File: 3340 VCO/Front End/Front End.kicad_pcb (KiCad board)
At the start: 2 copper layers, 60.6 x 104.5 mm, 32 parts, among them J1 AudioJack2_SwitchT, J2 AudioJack2_SwitchT, J3 AudioJack2_SwitchT, J4 AudioJack2_SwitchT, J5 AudioJack2_SwitchT, J6 Conn_01x19, J7 AudioJack2_SwitchT, J8 AudioJack2_SwitchT, J9 AudioJack2_SwitchT, SW1 SW_SPDT

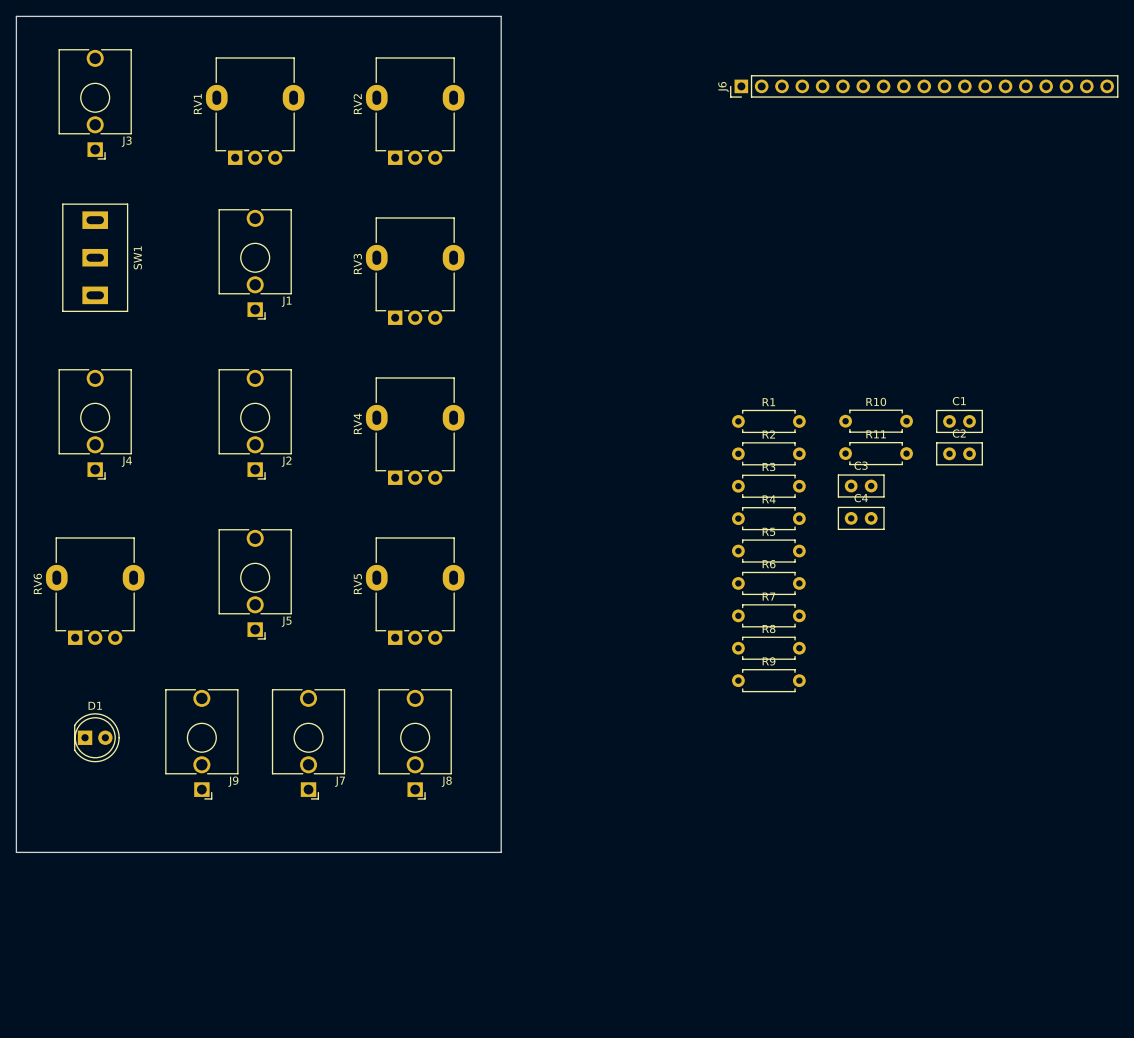
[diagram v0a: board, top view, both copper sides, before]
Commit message: Arrange VCO front end components
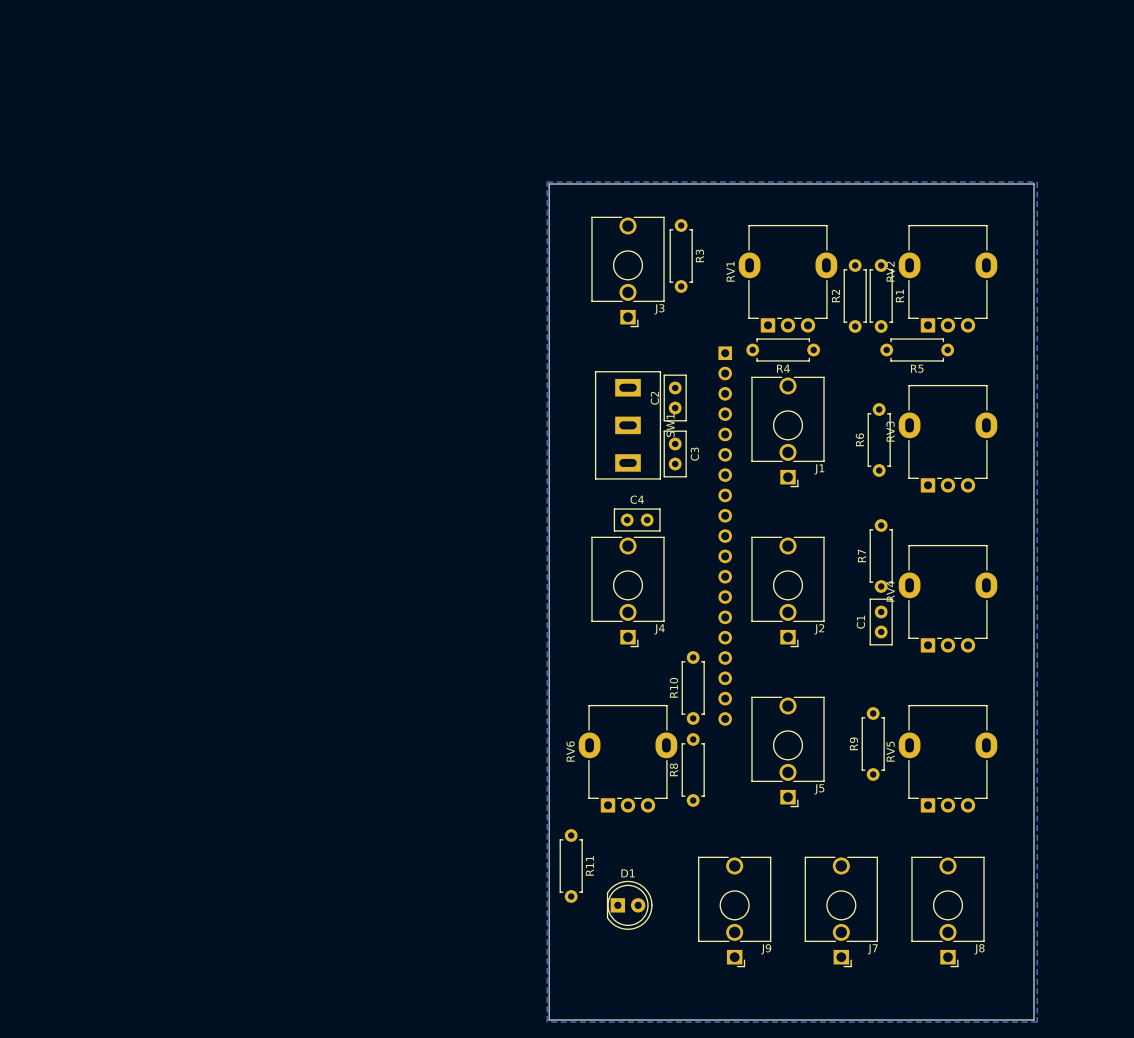
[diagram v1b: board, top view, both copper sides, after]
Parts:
- J6: moved to B.Cu
- moved D1 69.8 mm to (112.3, 137.4)
- moved J1 69.8 mm to (133.6, 83.8)
- moved J2 69.8 mm to (133.6, 103.8)
- moved J3 69.8 mm to (113.6, 63.9)
- moved J4 69.8 mm to (113.6, 103.8)
- moved J5 69.8 mm to (133.6, 123.8)
- moved J8 69.8 mm to (153.6, 143.8)
- moved J9 69.8 mm to (126.9, 143.8)
- moved RV1 69.8 mm to (131.1, 64.9)
- moved RV2 69.8 mm to (151.1, 64.9)
- moved RV3 69.8 mm to (151.1, 84.9)
- moved RV4 69.8 mm to (151.1, 104.9)
- moved RV5 69.8 mm to (151.1, 124.9)
- moved RV6 69.8 mm to (111.1, 124.9)
- moved SW1 69.8 mm to (113.6, 77.4)
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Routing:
- added copper zone on B.Cu, net Chassis

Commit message: Update VCO capacitor selection
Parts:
- added H1: MNT_STANDOFF, 0_MountingHole:MountingHole_Pitch7.5mm_Drill3.4mm, F.Cu at (109.5, 146.2)
- added H2: MNT_STANDOFF, 0_MountingHole:MountingHole_Pitch7.5mm_Drill3.4mm, F.Cu at (143.0, 70.5)
- C2: footprint 0_Capacitor_THT:C_Disc_D5.5mm_W2.5mm_P2.50mm -> 0_Capacitor_THT:C_Rect_L7.2mm_W4.5mm_P5.00mm
- C3: footprint 0_Capacitor_THT:C_Disc_D5.5mm_W2.5mm_P2.50mm -> 0_Capacitor_THT:C_Rect_L7.5mm_W5.5mm_P5.00mm
- moved R5 4.01 mm to (157.6, 68.2)
- moved C3 1.75 mm to (121.2, 79.8)
- moved C2 1.51 mm to (121.0, 75.0)
- moved R6 1.05 mm to (145.0, 84.1)
- moved J6 0.50 mm to (126.2, 68.3)
- moved R4 0.25 mm to (137.1, 68.0)

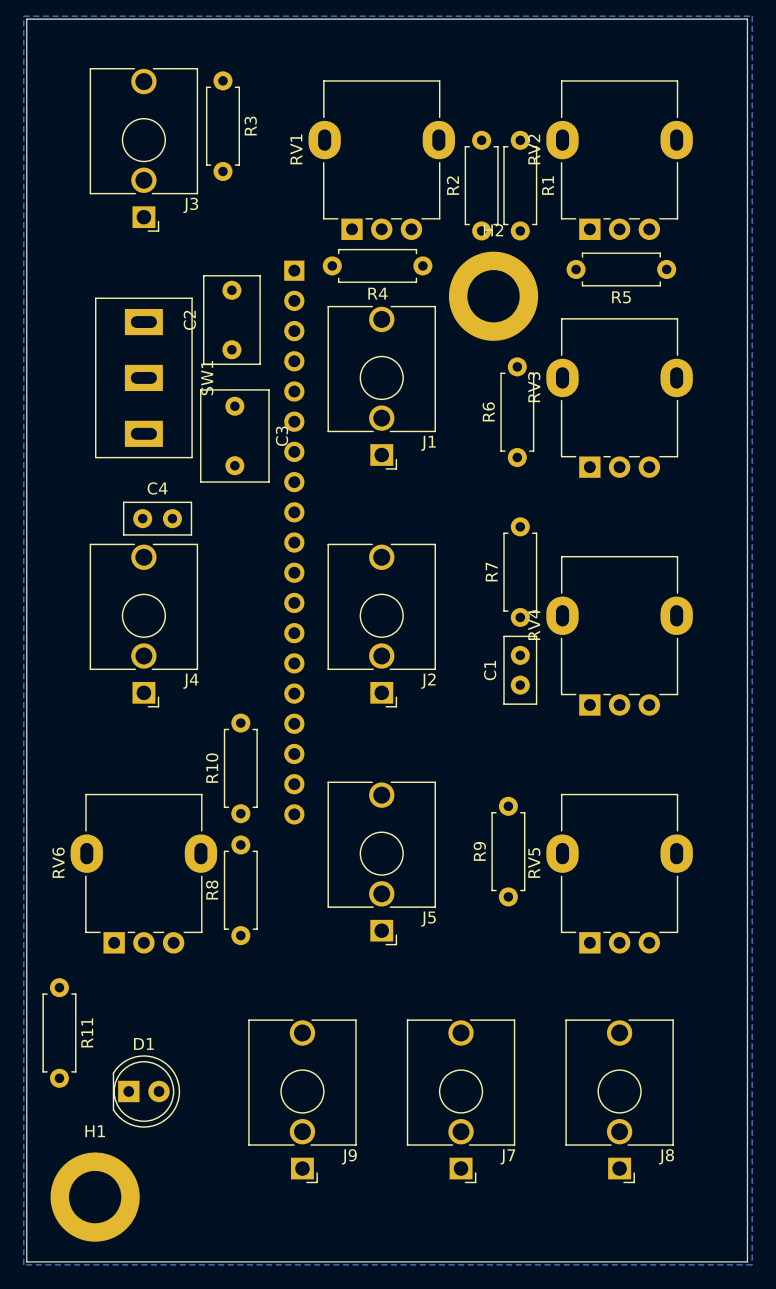
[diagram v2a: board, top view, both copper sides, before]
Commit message: Update gitignore, VCO changes
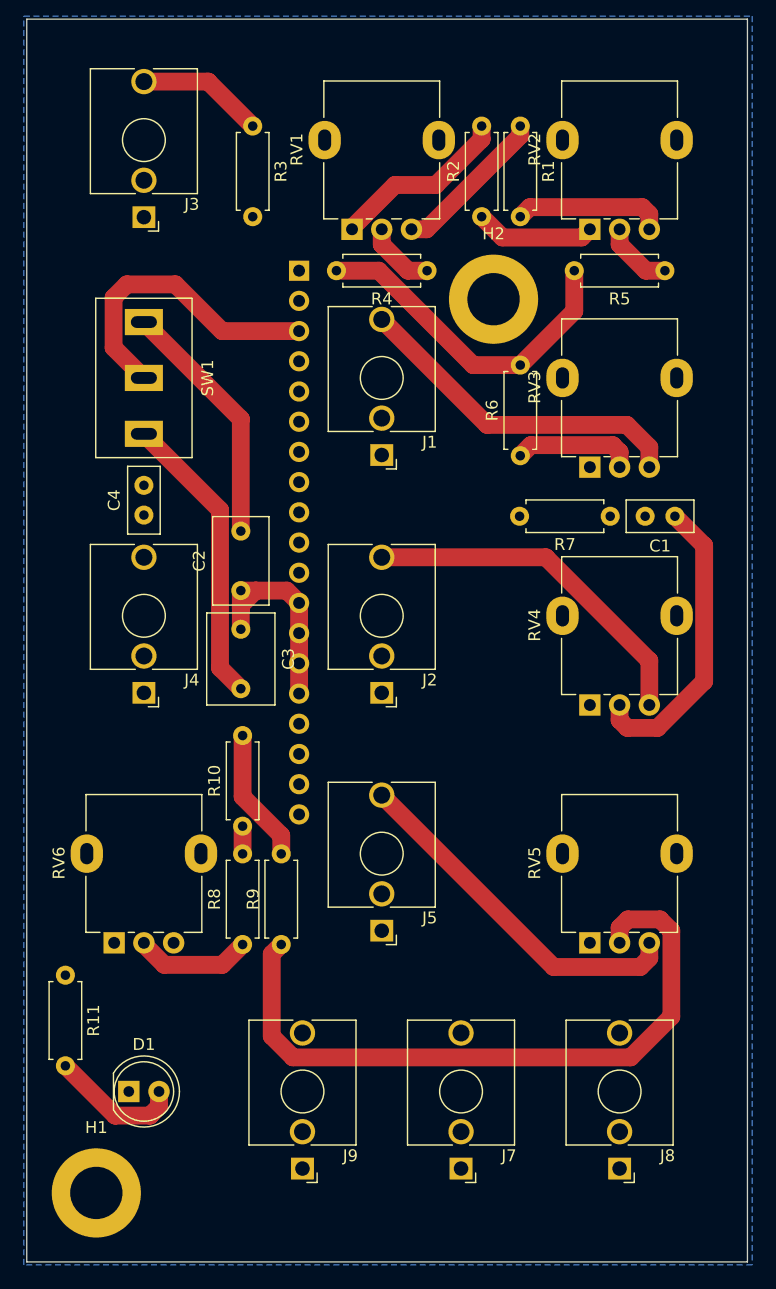
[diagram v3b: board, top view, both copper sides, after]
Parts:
- moved C2 20.3 mm to (121.8, 95.2)
- moved R9 19.5 mm to (125.2, 125.0)
- moved C1 19.3 mm to (158.2, 89.0), turned to 180 degrees
- moved C3 18.8 mm to (121.8, 98.5)
- moved R7 11.4 mm to (152.8, 89.0), turned to 180 degrees
- moved R3 4.55 mm to (122.8, 56.2)
- moved R1 1.20 mm to (145.2, 56.2)
- moved R2 1.20 mm to (142.0, 63.8)
- moved R11 1.16 mm to (107.0, 127.6)
- moved R10 1.06 mm to (121.9, 115.1)
- moved R8 0.76 mm to (121.9, 125.0)
- moved R4 0.53 mm to (137.4, 68.3)
- moved J6 0.40 mm to (126.7, 68.3)
- moved H1 0.36 mm to (109.6, 145.9)
- moved C4 0.32 mm to (113.6, 88.9), turned to 90 degrees
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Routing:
- net Net-(R9-Pad1): track 0.00 -> 57.3 mm
- net Net-(J5-PadT): track 0.00 -> 30.1 mm
- net Net-(J2-PadT): track 0.00 -> 29.8 mm
- net Net-(J1-PadT): track 0.00 -> 28.6 mm
- net /CV: track 0.00 -> 28.6 mm
- net /CAP: track 0.00 -> 25.5 mm
- net Net-(C1-Pad1): track 0.00 -> 25.2 mm
- net Net-(SW1-A): track 0.00 -> 24.8 mm
- net Net-(SW1-C): track 0.00 -> 21.0 mm
- net GND: track 0.00 -> 18.2 mm
- net -12V: track 0.00 -> 15.2 mm
- net +12V: track 0.00 -> 13.2 mm
- net Net-(R1-Pad2): track 0.00 -> 12.7 mm
- net /PWM: track 0.00 -> 11.3 mm
- net Net-(D1-A): track 0.00 -> 11.2 mm
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
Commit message: Finish VCO
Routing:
- net GND: track 18.2 -> 133.3 mm, vias 0 -> 2
- net +12V: track 13.2 -> 95.1 mm
- net -12V: track 15.2 -> 91.5 mm, vias 0 -> 1
- net /RAMP: track 0.00 -> 69.7 mm, vias 0 -> 1
- net /PULSE: track 0.00 -> 60.8 mm, vias 0 -> 1
- net /TRI: track 0.00 -> 58.1 mm, vias 0 -> 1
- net /LED: track 0.00 -> 52.6 mm, vias 0 -> 1
- net /HS: track 0.00 -> 42.3 mm, vias 0 -> 2
- net /PWM: track 11.3 -> 43.0 mm
- net /FM_LIN: track 0.00 -> 27.0 mm, vias 0 -> 1
- net /CV: track 28.6 -> 37.9 mm
- net Net-(J5-PadT): track 30.1 -> 35.3 mm, vias 0 -> 1
- net Net-(C4-Pad1): track 0.00 -> 3.55 mm
- net Net-(J2-PadT): track 29.8 -> 33.1 mm, vias 0 -> 1
- net Net-(C1-Pad2): track 0.00 -> 2.94 mm
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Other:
- board text added: "JLCJLCJLCJLC"
